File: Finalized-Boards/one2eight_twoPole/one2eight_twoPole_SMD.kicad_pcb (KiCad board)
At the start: 4 copper layers, 49.5 x 12 mm, 20 parts

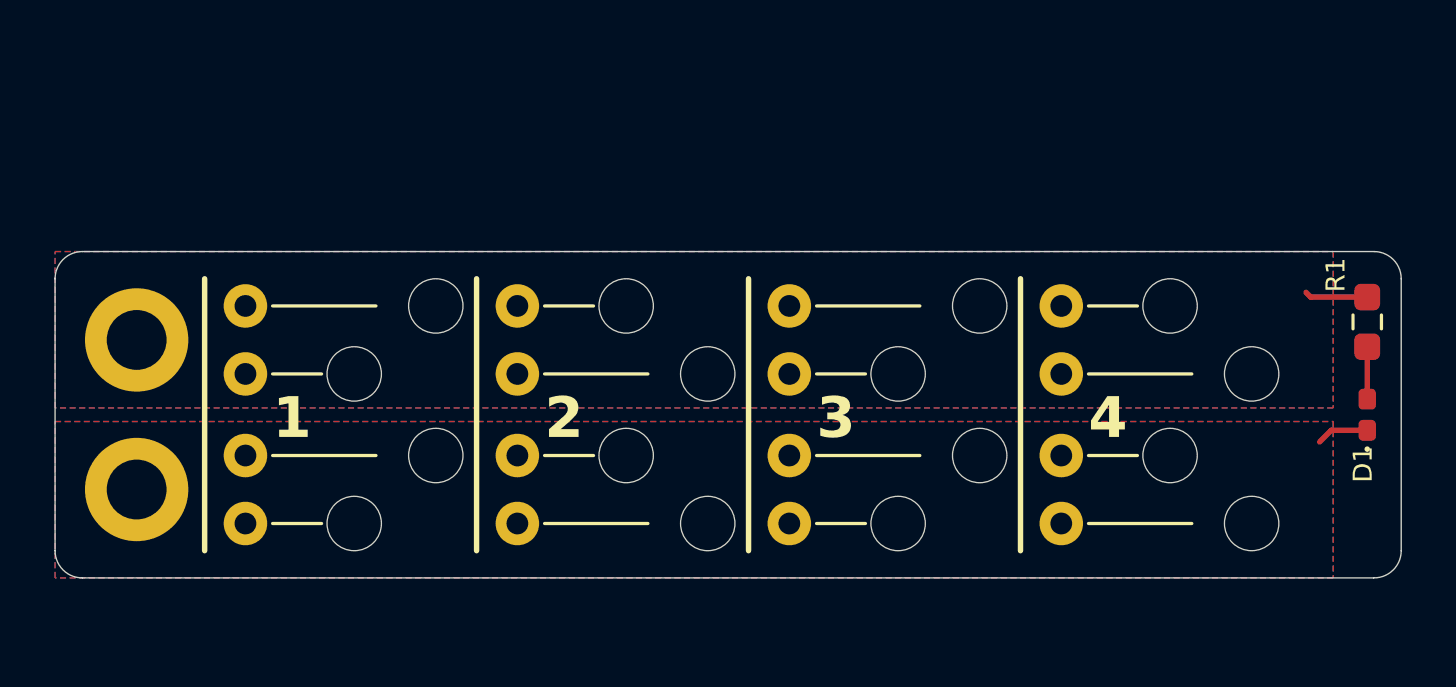
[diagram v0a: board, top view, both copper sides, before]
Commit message: Apply Matt's review changes to RTM, fanout and SRAM boards
SRAM: serial -> IDL_26_007 RevC - 09/2026 - CK/RS; vias untented (board-level);
GND zone 0.4 clearance / 0.1524 min width; In2 +3.3V stripe pulled back from
both board edges (tips 103.25 / 126.05) with 45-degree miters; +3.3V via moved
to (165.54, 125.92) and re-routed on F.Cu/B.Cu to clear GND (was 2 DRC errors);
C1/C2 0402 -> 0603 X7R in schematic and PCB; orphan teardrop + 2 zero-length
tracks removed.
Fanout: Matt's reworked layout (12 AWG input centred, both-side labels, 3 mm
shorter test points, D1/R1 as real reference designators, silk moved clear).
RTM: four 1812 1 A PPTCs, one per output; +5V pour full-board on F.Cu/In2,
GND on B.Cu/In1; 3.4 mm fused traces; zones extended past Edge.Cuts.
Removed stale pre-review gerbers/drills/layer PDFs (duplicates of Chris-Originals).
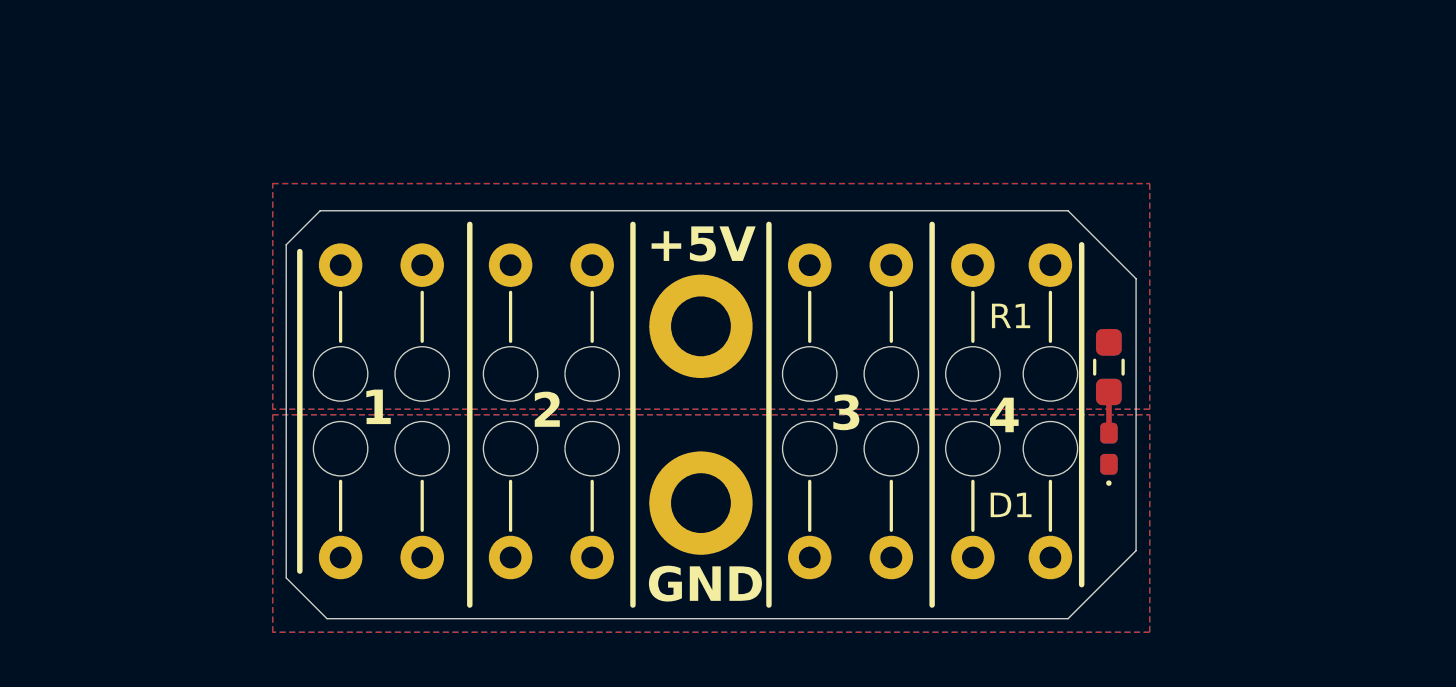
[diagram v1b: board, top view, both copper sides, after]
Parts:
- TP10, TP12, TP14, TP16, TP4, TP6, TP8: footprint 1_klm-sram-exp-lib:SolderWire-0.5sqmm_1x01_D0.9mm_OD2.1mm_Relief -> 1_klm-sram-exp-lib:SolderWire-0.5sqmm_1x01_D0.9mm_OD2.1mm_Relief_3mm_shorter_version
- TP18: footprint 1_My_footprint_lib:SolderWire-0.5sqmm_1x01_D0.9mm_OD2.1mm_Relief -> 1_klm-sram-exp-lib:SolderWire-0.5sqmm_1x01_D0.9mm_OD2.1mm_Relief_3mm_shorter_version
- moved TP5 29.9 mm to (136.6, 100.5), turned to 0 degrees
- moved TP9 29.6 mm to (136.6, 111.2), turned to 180 degrees
- moved TP10 27.0 mm to (133.8, 111.2), turned to 180 degrees
- moved TP6 26.8 mm to (133.8, 100.5), turned to 0 degrees
- moved TP15 26.8 mm to (110.5, 111.2), turned to 180 degrees
- moved TP11 26.5 mm to (110.5, 100.5), turned to 0 degrees
- moved TP12 23.8 mm to (113.5, 100.5), turned to 0 degrees
- moved TP16 23.5 mm to (113.5, 111.2), turned to 180 degrees
- moved TP1 20.8 mm to (123.8, 102.8)
- moved TP2 20.8 mm to (123.8, 109.2)
- moved TP3 13.8 mm to (130.8, 100.5), turned to 0 degrees
- moved TP8 13.8 mm to (130.8, 111.2), turned to 180 degrees
- moved TP4 11.5 mm to (127.8, 100.5), turned to 0 degrees
- moved TP7 11.4 mm to (127.8, 111.2), turned to 180 degrees
- moved TP13 11.0 mm to (116.8, 100.5), turned to 0 degrees
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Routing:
- net +5V: track 2.32 -> 0.00 mm
- net Earth: track 1.93 -> 0.00 mm
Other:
- board size 49.5 x 12 mm -> 31.2 x 15 mm
- board text added: "2026-09"
- board text added: "CK/RS/mza"
- board text added: "IDL_26_025"
- board text added: "for KLM SRAM"
- board text added: "power fanout revA"
- board text removed: "D1"
- board text removed: "R1"

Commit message: Matt's 9/17 review: RTM paired 5V/GND terminals, SRAM R1/R2 to 0603, fanout per-destination polyswitches; archive 9/16 boards
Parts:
- added F1: MF-MSMF110/16-2, Fuse:Fuse_1812_4532Metric, F.Cu at (112.0, 97.6)
- added F2: MF-MSMF110/16-2, Fuse:Fuse_1812_4532Metric, F.Cu at (118.2, 97.6)
- added F3: MF-MSMF110/16-2, Fuse:Fuse_1812_4532Metric, F.Cu at (129.2, 97.6)
- added F4: MF-MSMF110/16-2, Fuse:Fuse_1812_4532Metric, F.Cu at (135.2, 97.6)
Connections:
- TP11 pad 1: +5V -> +5VF1
- TP12 pad 1: +5V -> +5VF1
- TP13 pad 1: +5V -> +5VF2
- TP14 pad 1: +5V -> +5VF2
- TP3 pad 1: +5V -> +5VF3
- TP4 pad 1: +5V -> +5VF3
- TP5 pad 1: +5V -> +5VF4
- TP6 pad 1: +5V -> +5VF4
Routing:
- added copper zone on B.Cu, net +5VF1
- added copper zone on F.Cu, net +5VF1
- added copper zone on In1.Cu, net +5VF1
- added copper zone on In2.Cu, net +5VF1
- added copper zone on B.Cu, net +5VF2
- added copper zone on F.Cu, net +5VF2
- added copper zone on In1.Cu, net +5VF2
- added copper zone on In2.Cu, net +5VF2
- added copper zone on B.Cu, net +5VF3
- added copper zone on F.Cu, net +5VF3
- added copper zone on In1.Cu, net +5VF3
- added copper zone on In2.Cu, net +5VF3
- added copper zone on B.Cu, net +5VF4
- added copper zone on F.Cu, net +5VF4
- added copper zone on In1.Cu, net +5VF4
- added copper zone on In2.Cu, net +5VF4
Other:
- board size 31.2 x 15 mm -> 31.2 x 19.5 mm
- board text added: "power fanout revB"
- board text removed: "power fanout revA"

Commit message: Polyswitches sized to load: RTM F1-F4 MF-MSMF110/16-2 -> MF-MSMF030-2 (0.3 A), fanout F1-F4 -> MF-MSMF010-2 (0.1 A); refresh renders and DRC
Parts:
- F1, F2, F3, F4: value MF-MSMF110/16-2 -> MF-MSMF010-2
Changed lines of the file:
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@@
 			)
 		)
-		(property "Value" "MF-MSMF110/16-2"
+		(property "Value" "MF-MSMF010-2"
 			(at 0 2.65 0)
 			(layer "F.Fab")
@@
 			)
 		)
-		(property "Value" "MF-MSMF110/16-2"
+		(property "Value" "MF-MSMF010-2"
 			(at 0 2.65 0)
 			(layer "F.Fab")
@@
 			)
 		)
-		(property "Value" "MF-MSMF110/16-2"
+		(property "Value" "MF-MSMF010-2"
 			(at 0 2.65 0)
 			(layer "F.Fab")
@@
 			)
 		)
-		(property "Value" "MF-MSMF110/16-2"
+		(property "Value" "MF-MSMF010-2"
 			(at 0 2.65 0)
 			(layer "F.Fab")

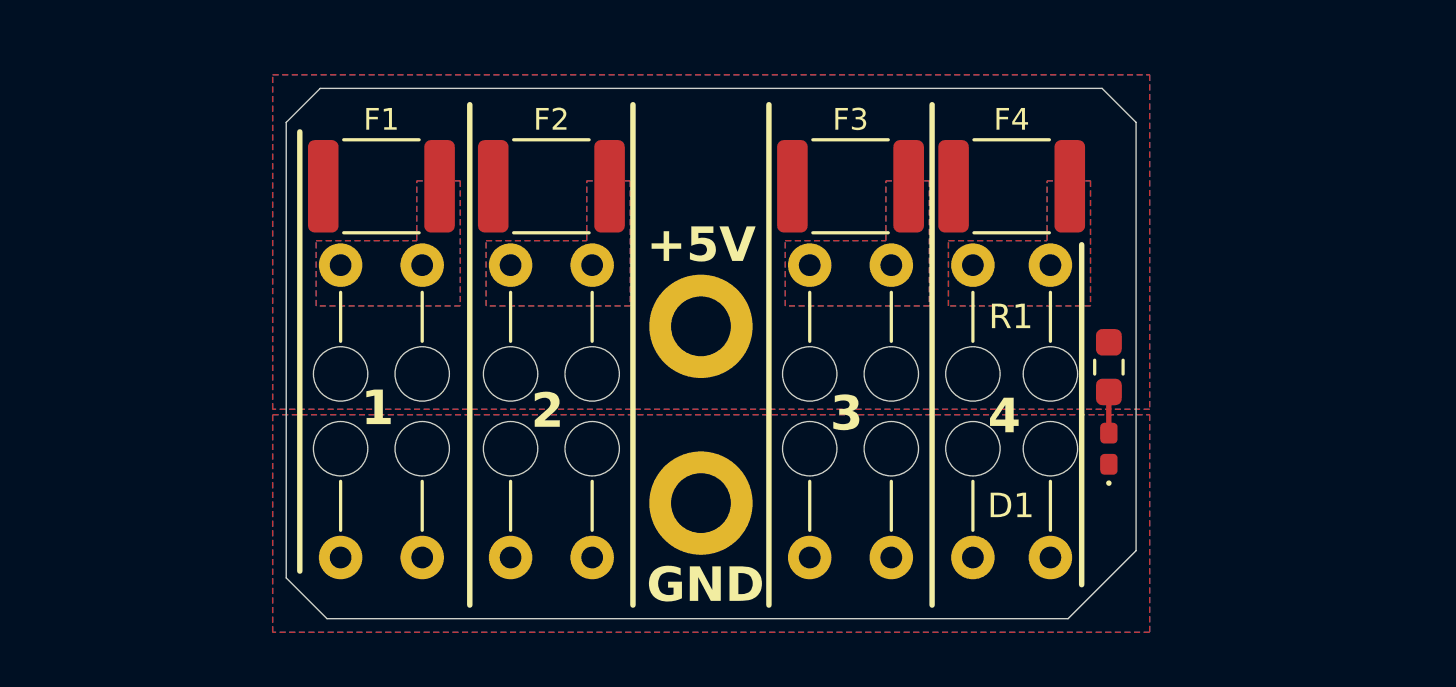
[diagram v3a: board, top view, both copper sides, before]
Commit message: Matt's 9/22 review: fanout fuses rotated, thermal-relief zones, stitching vias; SRAM footprints synced with library, sch/pcb parity fixed; add lib tables, schematic PDFs, full-severity DRC/ERC reports
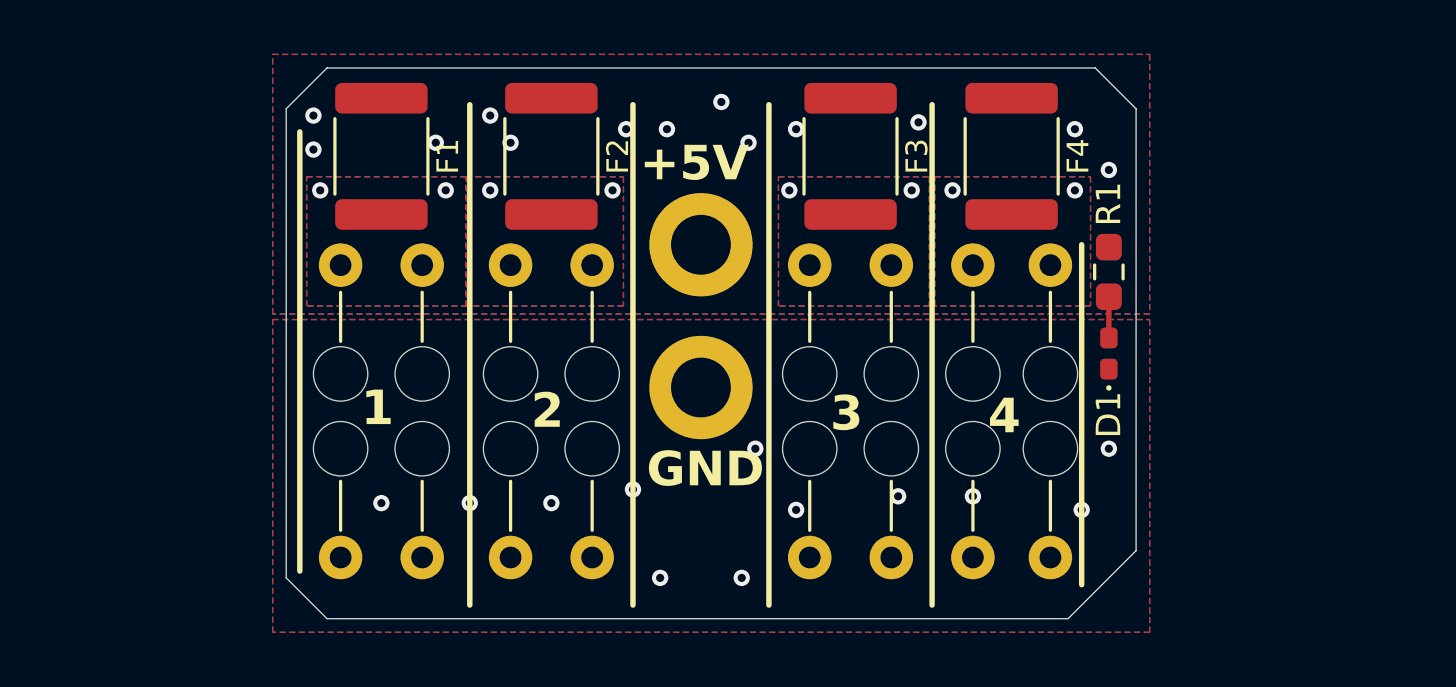
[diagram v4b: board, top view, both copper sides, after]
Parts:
- moved TP2 4.25 mm to (123.8, 105.0)
- moved D1 3.50 mm to (138.8, 103.8)
- moved R1 3.50 mm to (138.8, 100.8)
- moved TP1 3.00 mm to (123.8, 99.8)
- moved F1 1.10 mm to (112.0, 96.5), turned to -90 degrees
- moved F2 1.10 mm to (118.2, 96.5), turned to -90 degrees
- moved F3 1.10 mm to (129.2, 96.5), turned to -90 degrees
- moved F4 1.10 mm to (135.2, 96.5), turned to -90 degrees
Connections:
- net +5VF1 renamed /+5VF1
- net +5VF2 renamed /+5VF2
- net +5VF3 renamed /+5VF3
- net +5VF4 renamed /+5VF4
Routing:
- net Earth: vias 0 -> 12
- net /+5VF4: vias 0 -> 2
- net /+5VF3: vias 0 -> 2
- net /+5VF2: vias 0 -> 2
- net /+5VF1: vias 0 -> 2
- net +5V: vias 0 -> 13
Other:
- board size 31.2 x 19.5 mm -> 31.2 x 20.2 mm
- board text added: "2026-09-22"
- board text added: "KLM SRAM power fanout revB"
- board text removed: "2026-09"
- board text removed: "for KLM SRAM"
- board text removed: "power fanout revB"
